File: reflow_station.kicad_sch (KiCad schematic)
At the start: 110 parts, among them U1 L7805

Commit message: feat: redesign power from linear regulated with trafo to using buck converters
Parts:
- removed C2, C? (x2): 1000u, symbol Device:C_Polarized
- removed C3: 330n, symbol Device:C
- removed C4, C? (x5): 100n, symbol Device:C
- removed C?: 10u, symbol Device:C_Polarized
- removed C? (x3): C, symbol Device:C
- removed C?: 10n, symbol Device:C
- removed D? (x2): 1N4007, Diode_THT:D_DO-41_SOD81_P10.16mm_Horizontal, symbol Diode:1N4007
- removed D?: 1N4001, Diode_THT:D_DO-41_SOD81_P10.16mm_Horizontal, symbol Diode:1N4001
- removed IC?: ST1S41PHR, reflow_station_library:SOIC127P600X170-9N, symbol reflow_station_symbols:ST1S41PHR
- removed L?: L, symbol Device:L
- removed R2: 1k 0.5W, symbol Device:R
- removed R? (x8): R, symbol Device:R
- removed R? (x2): 10k, symbol Device:R
- removed R?: 200, symbol Device:R
- removed R? (x4): 100k, symbol Device:R
- removed R? (x3): 1k, symbol Device:R
- removed TH?: Thermistor, symbol Device:Thermistor
- removed TR1: TSZZ 3/007MP 230V 12V 0.25A, Transformer_THT:Transformer_Breve_TEZ-38x45, symbol Transformer:TEZ6.0-D-1
- removed U1: L7805, Package_TO_SOT_THT:TO-220-3_Vertical, symbol Regulator_Linear:L7805
- removed U? (x5): LM339, symbol Comparator:LM339
- removed U?: STM32F429IGTx, Package_QFP:LQFP-176_24x24mm_P0.5mm, symbol MCU_ST_STM32F4:STM32F429IGTx
- added C?: 470p, symbol Device:C
- added C? (x2): 100n, symbol Device:C
- added C?: 3.3n, symbol Device:C
- added C?: 4.7u, symbol Device:C_Polarized
- added C? (x2): C, symbol Device:C
- added C? (x3): 10u, symbol Device:C
- added C?: 220u, symbol Device:C_Polarized
- added C?: 10n, symbol Device:C
- added C?: 47u 25V, symbol Device:C
- added C?: 100n 25V, Capacitor_SMD:C_0603_1608Metric_Pad1.08x0.95mm_HandSolder, symbol Device:C
- added D? (x2): D, symbol Device:D
- added D?: LED, symbol Device:LED
- added IC?: AMC23C10DWVR, SOIC127P1150X280-8N, symbol reflow_station_symbols:AMC23C10DWVR
- added IC?: MP100LGN-Z, reflow_station_library:SOIC127P600X170-9N, symbol reflow_station_symbols:MP100LGN-Z
- added P?: IEC_60320_C13_Plug, symbol Connector:IEC_60320_C13_Plug
- added R?: 90.9k 1%, symbol Device:R
- added R?: 1k, Resistor_SMD:R_0402_1005Metric, symbol Device:R
- added R? (x3): R, symbol Device:R
- added R? (x3): 1.09M 1%, symbol Device:R
- added R? (x2): 100k, symbol Device:R
- added R?: 10.2k 1%, symbol Device:R
- added SW? (x2): SW_DPST_x2, symbol Switch:SW_DPST_x2
- added U? (x2): AMS1117-3.3, Package_TO_SOT_SMD:SOT-223-3_TabPin2, symbol Regulator_Linear:AMS1117-3.3
- added U?: RAC10-12SK/277, RAC10-K/277_SINGLE_RCP, symbol reflow_station_symbols:RAC10-12SK_277
- added U?: STM32F429ZITx, Package_QFP:LQFP-144_20x20mm_P0.5mm, symbol MCU_ST_STM32F4:STM32F429ZITx
- added U?: TPS82130, Package_LGA:Texas_SIL0008D_MicroSiP-8-1EP_2.8x3mm_P0.65mm_EP1.1x1.9mm_ThermalVias, symbol Converter_DCDC:TPS82130
- C1: footprint (none) -> Capacitor_THT:C_Axial_L12.0mm_D6.5mm_P15.00mm_Horizontal
- D1: value MBL110S -> MBL10S; footprint reflow_station_library:Bridge_C2488 -> reflow_station_library:MBS_L4.7-W3.8-P2.40-LS7.0-TL
- F1: value Fuse 40mA -> Fuse 15A
- R1: value 100 -> 100 3W
- R?: value 330 -> 1k; footprint (none) -> Resistor_SMD:R_0402_1005Metric
- R? (x2): value 1k -> 680
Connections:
- net AC_REF is gone; now on net N: D1.2
- net +12V: now also R?.1, C?.1, C?.1, C?.1, U?.1 (EN), U?.2 (VIN), U?.5 (+VOUT)
- net +5V: now also C?.1, C?.1, C?.1, C?.1, C?.1, C?.1, R?.1, R?.1, U?.3 (VI), U?.4 (VOUT), U?.5 (VOUT); no longer R?.1
- net GND: now also C?.2, C?.2, C?.2, C?.2, C?.2, C?.2, C?.2, C?.2, C?.2, C?.2, C?.2, D?.1 (K), R?.2, U?.1 (GND), U?.3 (GND), U?.4 (-VOUT), U?.9 (GND); no longer D1.4 (-)
- net L: now also SW?.4 (B)
- net L_FUSED: now also D1.3, R?.1, U?.2 (VAC_IN(L))
- net N: now also C?.2, D?.1 (K), D?.2 (A), IC?.3 (INN), SW?.2 (B), U?.1 (VAC_IN(N))
- net L_RECTIFIED: now reaches D1.1 (+)
- net L_RECTIFIED: now also IC?.8 (VIN)
- new net: C?.1, IC?.3 (FB), R?.2, R?.2
- new net: C?.1, R?.1, U?.2 (VO)
- new net: C?.1, IC?.2 (INP), R?.2
- new net: C?.1, U?.8 (SS/TR)
- new net: U?.107 (VSS), U?.120 (VSS), U?.130 (VSS), U?.16 (VSS), U?.38 (VSS), U?.51 (VSS), U?.61 (VSS), U?.83 (VSS), U?.94 (VSS)
- new net: R?.1, R?.2, U?.6 (FB)
- new net: D?.1 (K), D?.2 (A), R?.1, R?.2
- new net: C?.1, IC?.5 (VD), IC?.6 (VB)
- new net: R?.1, R?.2 (x2)
- new net: R?.2, U?.7 (PG)
- new net: IC?.1 (PG), R?.1
- new net +12V_ISOLATED: C?.1, C?.1, C?.2, IC?.1 (VDD1), IC?.4 (VOUT), R?.1, R?.2
- new net +3V3: D?.2 (A), R?.2
- new net Earth: P?.3 (PE)
- new net GND1: C?.2, C?.2, C?.2, D1.4 (-), IC?.2 (GND), IC?.4 (GND1), IC?.9 (EP), R?.1
- new net L_IN: P?.2 (L), SW?.3 (A)
- new net N_IN: P?.1 (N), SW?.1 (A)
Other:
- note added: "+12V power consumption: - +5V power consumption (500mA): 2.5W - +3.3V power consumption (600mA): 2.0W - fans: 1.0W ----------------------------------------- TOTAL: 5.5W"
- note added: "+3.3V power consumption: - LCD (363mA): 1.2W - MCU (270mA): 0.9W - LED TRIAC (15mA): 0.04W - Thermocoup (600uA): 0.001W"
- note added: "+5V power consumption: - LED(PWR): 5mA - USB: 500mA"
- note added: "230VAC power consumption: - +12V power consumption: 5.5W - Heaters power consumption: 3000W ------------------------------------ TOTAL: 3006W"
- note added: "SWD"
- note removed: "+12V is power supply for the fans. It does not have to be as stable as linear regulated power supply for the MCU and peripherals."
- note removed: "The termistor should be placed as close to the transformer as possible."
- moved on the sheet: C1, C?, D1, D?, F1, J?, Q?, R1, R?, TC?, U?

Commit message: feat: add all peri
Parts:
- removed U?: AMS1117-3.3, Package_TO_SOT_SMD:SOT-223-3_TabPin2, symbol Regulator_Linear:AMS1117-3.3
- added C? (x16): 100n, symbol Device:C
- added C? (x2): 1u, symbol Device:C
- added C?: 4.7u, symbol Device:C
- added C?: 47u, symbol Device:C
- added C? (x2): 2.2u, symbol Device:C
- added FL?: Common Mode Choke 90R 100MHz, symbol Filter:Choke_CommonMode_FerriteCore_1234
- added J? (x2): Conn_01x03, symbol Connector_Generic:Conn_01x03
- added J?: F52Q-1A7H1-11015, reflow_station_library:F52Q1A7H111015, symbol reflow_station_symbols:F52Q-1A7H1-11015
- added R?: 47k, symbol Device:R
- added U?: TPS2051BDBVR, DBV0005A_N, symbol reflow_station_symbols:TPS2051BDBVR
- added U?: RCLAMP0504F.TCT, reflow_station_library:SC70-6L_RCLAMP_SEM, symbol reflow_station_symbols:RCLAMP0504F.TCT
- C?: value C -> 2.2n
- R?: value R -> 10k
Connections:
- net +12V_ISOLATED: now also C?.2, C?.2
- net +3V3: now also IC?.8 (VDD2), U?.108 (VDD), U?.121 (VDD), U?.131 (VDD), U?.144 (VDD), U?.17 (VDD), U?.30 (VDD), U?.33 (VDDA), U?.39 (VDD), U?.52 (VDD), U?.62 (VDD), U?.72 (VDD), U?.84 (VDD), U?.95 (VDD), C?.1, C?.1, C?.1, C?.1, C?.1, C?.1, C?.1, C?.1, C?.1, C?.1, C?.1, C?.1, C?.1, C?.1, C?.1, J?.14, J?.15
- net +5V: now also C?.1, R?.2, U?.5 (IN)
- net GND: now also IC?.5 (GND2), J?.4 (GND), J?.SH (Shield), U?.107 (VSS), U?.120 (VSS), U?.130 (VSS), U?.16 (VSS), U?.31 (VSSA), U?.38 (VSS), U?.51 (VSS), U?.61 (VSS), U?.83 (VSS), U?.94 (VSS), C?.2, C?.2, C?.2, C?.2, C?.2, C?.2, C?.2, C?.2, C?.2, C?.2, C?.2, C?.2, C?.2, C?.2, C?.2, C?.2, C?.2, C?.2, C?.2, C?.2, J?.1, J?.10, J?.13, J?.2 (Pin_2), J?.3 (Pin_3), J?.4, J?.7, J?.MP1, J?.MP2, J?.MP3, J?.MP4, U?.2, U?.2 (GND)
- net GND1: now also C?.1, C?.1
- net AC_SYNC: now reaches IC?.7 (OUT2)
- net at U?.106 (VCAP_2): now also C?.1
- net at U?.71 (VCAP_1): now also C?.1
- net at J?.1 (VBUS): now also C?.1, C?.1, U?.1 (OUT), U?.5
- net at J?.2 (D-): now also FL?.3, U?.1
- net at J?.3 (D+): now also FL?.1, U?.6
- new net: R?.1, U?.3 (OC_N)
- new net DSI1_CN: J?.5
- new net DSI1_CP: J?.6
- new net DSI1_DN0: J?.8
- new net DSI1_DN1: J?.2
- new net DSI1_DP0: J?.9
- new net DSI1_DP1: J?.3
- new net SCL0: J?.11
- new net SDA0: J?.12
- new net SWCLK: J?.1 (Pin_1)
- new net SWDIO: J?.3 (Pin_3)
- new net UART_RX: J?.1 (Pin_1)
- new net UART_TX: J?.2 (Pin_2)
- new net USB_D+: FL?.2
- new net USB_D-: FL?.4
- new net USB_EN: U?.4 (EN)
- no-connect marks 0 -> 1
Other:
- note added: "SWD & UART"
- note removed: "SWD"
- moved on the sheet: C?, D?, J?, R?, U?

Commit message: fix: replace voltage regulator with modern LDO with automotive qc
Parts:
- removed M?: Fan_CPU_4pin, symbol Motor:Fan_CPU_4pin
- removed U?: AMS1117-3.3, Package_TO_SOT_SMD:SOT-223-3_TabPin2, symbol Regulator_Linear:AMS1117-3.3
- added C?: 10n, symbol Device:C
- added U?: TPS79633QDCQRQ1, reflow_station_library:DCQ0006A_N, symbol reflow_station_symbols:TPS79633QDCQRQ1
- C?: value 10u -> 2.2u
- C?: value 10u -> 1u
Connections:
- net +5V: now also U?.1 (EN), U?.2 (IN)
- net GND: now also C?.2, U?.3 (GND), U?.6 (GND)
- net at C?.1, R?.1: now also U?.4 (OUT)
- new net: C?.1, U?.5 (NR_FB)
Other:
- note added: "Depending on legacy part the 10n cap should be populated"
- note removed: "Reflow Fans"
- note removed: "Trafo Fan"
- moved on the sheet: C?, D1, D?, IC?, M?, R?

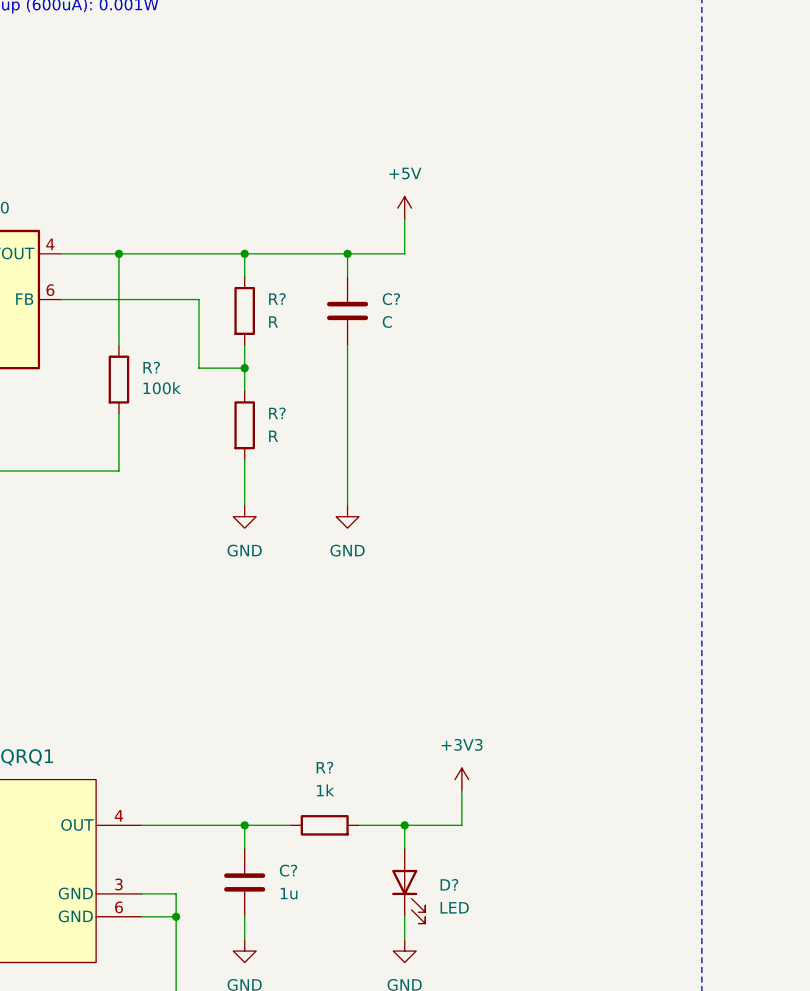
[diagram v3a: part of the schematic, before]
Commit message: fix: add power rails BEFORE signal diode resistor
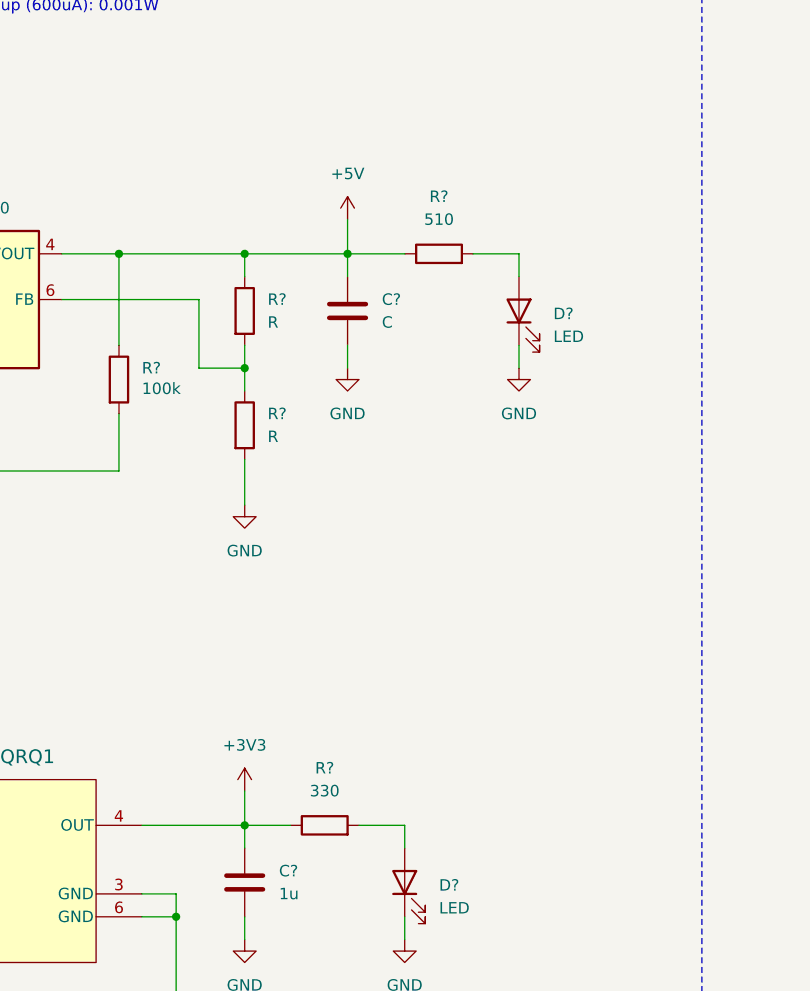
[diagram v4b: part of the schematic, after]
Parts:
- added D?: LED, symbol Device:LED
- added R?: 510, Resistor_SMD:R_0402_1005Metric, symbol Device:R
- R?: value 1k -> 330
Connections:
- net +3V3: now also C?.1, R?.1, U?.4 (OUT); no longer D?.2 (A), R?.2
- net +5V: now also R?.1
- net GND: now also D?.1 (K)
- new net: D?.2 (A), R?.2 (x2)

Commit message: feat: normalize power section to use one regulator type; add SWD 10 pin connector; add usb-uart IC; add control and signaling; separate heaters
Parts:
- removed C? (x5): 100n, symbol Device:C
- removed C?: 2.2u, symbol Device:C
- removed C?: 10n, symbol Device:C
- removed D? (x2): D, symbol Device:D
- removed FL?: Common Mode Choke 90R 100MHz, symbol Filter:Choke_CommonMode_FerriteCore_1234
- removed J? (x2): Conn_01x03, symbol Connector_Generic:Conn_01x03
- removed Q? (x2): BTA16-600B, Package_TO_SOT_THT:TO-220-3_Vertical, symbol Triac_Thyristor:BTA16-600B
- removed R? (x2): 220, symbol Device:R
- removed R? (x2): Heater, symbol Device:Heater
- removed R?: 680, symbol Device:R
- removed U?: RAC10-12SK/277, RAC10-K/277_SINGLE_RCP, symbol reflow_station_symbols:RAC10-12SK_277
- removed U?: MOC3023M, symbol Relay_SolidState:MOC3023M
- removed U?: STM32F429ZITx, Package_QFP:LQFP-144_20x20mm_P0.5mm, symbol MCU_ST_STM32F4:STM32F429ZITx
- removed U?: TPS79633QDCQRQ1, reflow_station_library:DCQ0006A_N, symbol reflow_station_symbols:TPS79633QDCQRQ1
- added C38, C? (x4): 100n, symbol Device:C
- added C39, C?: 1u, symbol Device:C
- added C? (x2): 10p, symbol Device:C
- added C? (x2): 1.5p, symbol Device:C
- added C?: 430p, symbol Device:C
- added C?: 10u, symbol Device:C
- added C?: 2.2u, symbol Device:C
- added D3: BAT54S, Package_TO_SOT_SMD:SOT-23, symbol Diode:BAT54S
- added D? (x6): LED, symbol Device:LED
- added J?: Conn_ARM_JTAG_SWD_10, Connector_PinHeader_1.27mm:PinHeader_2x05_P1.27mm_Vertical, symbol Connector:Conn_ARM_JTAG_SWD_10
- added L?: FCM1608KF-601T03, symbol Device:L
- added Q? (x3): BTA16-600B, Package_TO_SOT_THT:TO-220-3_Vertical, symbol Triac_Thyristor:BTA16-600B
- added R7: 10, symbol Device:R
- added R? (x6): 220, symbol Device:R
- added R?: 309k, symbol Device:R
- added R? (x3): 680, symbol Device:R
- added R? (x6): 330, Resistor_SMD:R_0402_1005Metric, symbol Device:R
- added R? (x2): 100k, symbol Device:R
- added R? (x3): Heater, symbol Device:Heater
- added R? (x2): 10k, symbol Device:R
- added SW? (x2): SW_SPST, symbol Switch:SW_SPST
- added SW? (x2): SW_SPDT, symbol Switch:SW_SPDT
- added SW?: SW_DIP_x08, symbol Switch:SW_DIP_x08
- added SW?: SW_Push, symbol Switch:SW_Push
- added TP? (x40): TestPoint, symbol Connector:TestPoint
- added U? (x3): MOC3023M, symbol Relay_SolidState:MOC3023M
- added U?: STM32F469VITx, Package_QFP:LQFP-100_14x14mm_P0.5mm, symbol MCU_ST_STM32F4:STM32F469VITx
- added U?: FT230XQ, Package_DFN_QFN:QFN-16-1EP_4x4mm_P0.65mm_EP2.1x2.1mm, symbol Interface_USB:FT230XQ
- added U?: TPS82130, Package_LGA:Texas_SIL0008D_MicroSiP-8-1EP_2.8x3mm_P0.65mm_EP1.1x1.9mm_ThermalVias, symbol Converter_DCDC:TPS82130
- added U?: RAC20-12SK, Converter_ACDC:Converter_ACDC_Recom_RAC20-xxSK_THT, symbol Converter_ACDC:RAC20-12SK
- added Y?: 32.768kHz, symbol Device:Crystal
- added Y?: 25MHz, symbol Device:Crystal
- C13: renamed from C?; value 1u -> 22u
- C3: renamed from C?; value C -> 47u
- C8: renamed from C?; value 3.3n -> 430p
- D4: renamed from D1; value MBL10S -> MB10S
- R3: renamed from R?; value R -> 523k
- R6: renamed from R?; value R -> 100k
- gave numbers to parts that had none: 97
- renumbered R1 to R4
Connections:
- net +12V: now also C?.1, TP?.1, U?.1 (EN), U?.2 (VIN), U?.5 (+Vout)
- net +12V_ISOLATED: now also R7.1, TP?.1; no longer C10.2, C9.2, IC1.1 (VDD1)
- net +3V3: now also C?.1, C?.1, C?.1, J?.1 (VTref), L?.1, R?.1, R?.1, SW?.3 (C), SW?.3 (C), TP?.1, U?.100 (VDD), U?.24 (VDD), U?.3 (VBAT), U?.4 (VOUT), U?.45 (VDD), U?.5 (VOUT), U?.55 (VDDDSI), U?.56 (VCAPDSI), U?.62 (VDD12DSI), U?.65 (VDDUSB), U?.77 (VDD), U?.8 (VDD)
- net +5V: now also R?.1, R?.1, R?.1, TP?.1
- net AC_SYNC: now also TP?.1
- net DSI1_CN: now also TP?.1, U?.61 (DSIHOST_CKN)
- net DSI1_CP: now also TP?.1, U?.60 (DSIHOST_CKP)
- net DSI1_DN0: now also TP?.1, U?.58 (DSIHOST_D0N)
- net DSI1_DN1: now also TP?.1, U?.64 (DSIHOST_D1N)
- net DSI1_DP0: now also TP?.1, U?.57 (DSIHOST_D0P)
- net DSI1_DP1: now also TP?.1, U?.63 (DSIHOST_D1P)
- net GND: now also C38.2, C39.2, C?.2, C?.2, C?.2, C?.2, C?.2, C?.2, C?.2, C?.2, C?.2, C?.2, C?.2, C?.2, D?.1 (K), D?.1 (K), D?.1 (K), D?.1 (K), D?.1 (K), D?.1 (K), J?.3 (GND), J?.5 (GND), J?.9 (GNDDetect), R?.2, SW?.1, SW?.1 (A), SW?.1 (A), U?.16 (VSSA), U?.2 (VSS), U?.23 (VSS), U?.3 (GND), U?.4 (-Vout), U?.4 (~{CTS}), U?.44 (VSS), U?.59 (VSSDSI), U?.7 (VSS), U?.78 (VSS), U?.9 (GND)
- net L: now also R?.1, R?.1, R?.1, R?.2, R?.2, R?.2
- net L_FUSED: now also U?.1 (AC(N))
- net N: now also D3.1 (A), D3.2 (K), Q?.1 (A1), Q?.1 (A1), Q?.1 (A1), U?.2 (AC(L))
- net SCL0: now also TP?.1
- net SDA0: now also TP?.1
- net SPI_TH1_CLK: now also TP?.1
- net SPI_TH1_MISO: now also TP?.1
- net SPI_TH1_MOSI: now also TP?.1
- net SPI_TH2_CLK: now also TP?.1
- net SPI_TH2_MISO: now also TP?.1
- net SPI_TH2_MOSI: now also TP?.1
- net SWCLK: now also J?.4 (SWCLK/TCK), TP?.1, U?.79 (PA14)
- net SWDIO: now also J?.2 (SWDIO/TMS), TP?.1, U?.75 (PA13)
- net UART_RX: now also TP?.1, U?.2 (RXD)
- net UART_TX: now also TP?.1, U?.15 (TXD)
- net USB_D+: now also J4.3 (D+), U10.6, TP?.1
- net USB_D-: now also J4.2 (D-), U10.1, TP?.1
- net at C40.2, C46.1, R35.2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: now also TP?.1
- net at C33.2, C35.1, R28.2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: now also TP?.1
- net at C11.1, IC1.2 (INP), R11.2: now also TP?.1
- net at C41.2, C47.1, R36.2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: now also TP?.1
- net at C32.2, C34.1, R27.2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: now also TP?.1
- net at C51.1, C52.1, J4.1 (VBUS)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: now also TP?.1
- net at C54.1: now also U?.76 (VCAP2)
- net at C53.1: now also U?.43 (VCAP1)
- net at R10.2, R11.1: now also D3.3 (COM)
- net BOTTOM_HEATER_ON renamed TOP_HEATER_B
- net TOP_HEATER_B: now also TP?.1
- new net: C10.2, C9.2, IC1.1 (VDD1), R7.2
- new net: R?.1, U?.6 (x3)
- new net: R?.1, R?.2, U?.6 (FB)
- new net: R?.2, U?.1 (x3)
- new net: D?.2 (A), R?.2 (x6)
- new net: C?.1, U?.6 (PC15), Y?.1
- new net: C?.1, TP?.1, U?.5 (PC14), Y?.2
- new net: C?.1, U?.10 (PH1), Y?.1
- new net: Q?.2 (A2), R?.2 (x3)
- new net: Q?.3 (G), R?.2 (x3)
- new net: R?.1, U?.4 (x3)
- new net: C?.1, TP?.1, U?.9 (PH0), Y?.2
- new net: R?.2, U?.7 (PG)
- new net: R?.2, SW?.2 (B)
- new net: R?.1, U?.31 (PB2)
- new net: R?.2, U?.97 (BOOT0)
- new net: U?.13 (GND), U?.17 (GND), U?.3 (GND)
- new net: R?.1, SW?.2 (B)
- new net: C?.1, U?.8 (SS/TR)
- new net +3.3VA: C38.1, C39.1, C?.1, C?.1, L?.2, TP?.1, U?.17 (VREF+), U?.18 (VDDA)
- new net BOTTOM_HEATER_A: TP?.1, U?.2
- new net BOTTOM_HEATER_B: TP?.1, U?.2
- new net RESET: C?.1, J?.10 (~{RESET}), SW?.2, TP?.1, U?.11 (NRST)
- new net SWO: J?.6 (SWO/TDO), TP?.1, U?.92 (PB3)
- new net TOP_HEATER_A: TP?.1, U?.2
- no-connect marks 1 -> 5
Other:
- note added: "+12V power consumption: - +5V power consumption (500mA): 2.5W - +3.3V power consumption (600mA): 2.0W - Fans: ___W ----------------------------------------- TOTAL: 4.5W + Fans"
- note added: "Bottom Heaters"
- note added: "Control Switches"
- note added: "Cooling"
- note added: "Failure"
- note added: "Heating"
- note added: "Run"
- note added: "SWD"
- note added: "Self Test"
- note added: "Signal Diodes"
- note added: "Stop"
- note added: "Top Heaters"
- note added: "USB - UART"
- note removed: "+12V power consumption: - +5V power consumption (500mA): 2.5W - +3.3V power consumption (600mA): 2.0W - fans: 1.0W ----------------------------------------- TOTAL: 5.5W"
- note removed: "Bottom Heater (preheat)"
- note removed: "Depending on legacy part the 10n cap should be populated"
- note removed: "SWD & UART"
- note removed: "Top Heater (main)"
- moved on the sheet: C10, C13, C19, C2, C20, C21, C22, C23, C24, C25, C26, C3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

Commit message: feat: wire usb to uart and add GNDA for thermocouples
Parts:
- added C? (x2): 47p, symbol Device:C
- added C? (x3): 100n, symbol Device:C
- added C?: 4.7u, symbol Device:C
- added D? (x2): LED, symbol Device:LED
- added J?: USB_C_Receptacle_USB2.0_16P, symbol Connector:USB_C_Receptacle_USB2.0_16P
- added R? (x9): 10k, symbol Device:R
- added R? (x2): 27, symbol Device:R
- added R? (x8): 0, symbol Device:R
- added R? (x2): 5.1k, symbol Device:R
- added R? (x2): 330, Resistor_SMD:R_0402_1005Metric, symbol Device:R
- added R?: 4.7k, symbol Device:R
- added SW?: SW_SPST, symbol Switch:SW_SPST
- added U? (x2): RCLAMP0504F.TCT, reflow_station_library:SC70-6L_RCLAMP_SEM, symbol reflow_station_symbols:RCLAMP0504F.TCT
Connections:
- net +3V3: now also U?.1 (VCCIO), U?.10 (VCC), U?.8 (3V3OUT), U?.9 (~{RESET}), C?.1, C?.1, C?.1, C?.1, D?.2 (A), D?.2 (A), R?.1, R?.1, R?.1, R?.1, R?.1, R?.1, R?.1, R?.1, U?.5
- net DSI1_CN: now also R?.1; no longer J1.5
- net DSI1_CP: now also R?.1; no longer J1.6
- net DSI1_DN0: now also R?.1; no longer J1.8
- net DSI1_DN1: now also R?.1; no longer J1.2
- net DSI1_DP0: now also R?.1; no longer J1.9
- net DSI1_DP1: now also R?.1; no longer J1.3
- net GND: now also SW?.10, SW?.11, SW?.12, SW?.13, SW?.14, SW?.15, SW?.16, SW?.9, U?.13 (GND), U?.17 (GND), U?.3 (GND), C?.2, C?.2, C?.2, C?.2, C?.2, C?.2, J?.A1 (GND), J?.A12 (GND), J?.B1 (GND), J?.B12 (GND), J?.SH (SHIELD), R?.1, R?.1, R?.2, U?.2, U?.2
- net SCL0: now also R?.1; no longer J1.11
- net SDA0: now also R?.1; no longer J1.12
- net SWCLK: now also U?.6
- net SWDIO: now also U?.1
- net SWO: now also U?.4
- net TOP_TRIAC_A_ON: now reaches SW?.1
- net TOP_TRIAC_A_ON: now also R?.2
- net TOP_TRIAC_B_ON: now reaches SW?.2
- net TOP_TRIAC_B_ON: now also R?.2
- net BOTTOM_TRIAC_A_ON: now reaches SW?.3
- net BOTTOM_TRIAC_A_ON: now also R?.2
- net BOTTOM_TRIAC_B_ON: now reaches SW?.4
- net BOTTOM_TRIAC_B_ON: now also R?.2
- net at SW?.5: now also R?.2
- net at SW?.6: now also R?.2
- net at SW?.7: now also R?.2
- net at SW?.8: now also R?.2
- net UART_TXLED: now reaches U?.11 (CBUS1)
- net UART_TXLED: now also R?.2
- net VBUS_SENSE: now reaches U?.12 (CBUS0)
- net VBUS_SENSE: now also R?.1, R?.2
- net UART_RXLED: now reaches U?.5 (CBUS2)
- net UART_RXLED: now also R?.2
- net at U?.6 (USBDP): now also R?.2
- net at U?.7 (USBDM): now also R?.2
- new net: C?.1, J?.A6 (D+), R?.1, U?.6
- new net: C?.1, J?.A7 (D-), R?.1, U?.1
- new net: J?.A4 (VBUS), J?.A9 (VBUS), J?.B4 (VBUS), J?.B9 (VBUS), R?.1, U?.5
- new net: J?.A5 (CC1), R?.2
- new net: J?.B5 (CC2), R?.2
- new net: J1.9, R?.2
- new net: J1.3, R?.2
- new net: D?.1 (K), R?.1 (x2)
- new net: J1.8, R?.2
- new net: J1.11, R?.2
- new net: J1.5, R?.2
- new net: J1.12, R?.2
- new net: J1.2, R?.2
- new net: J1.6, R?.2
- no-connect marks 5 -> 13
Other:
- note added: "Kill"
- note added: "Run / Resume"
- note added: "Stop & Hold"
- moved on the sheet: C33, C35, C37, C41, C44, C45, C47, C49, J1, J?, R26, R28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
